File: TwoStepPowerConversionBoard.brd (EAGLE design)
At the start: 66 x 71.1 mm, 49 parts, among them U3 AZ1117EH-3.3TRG1

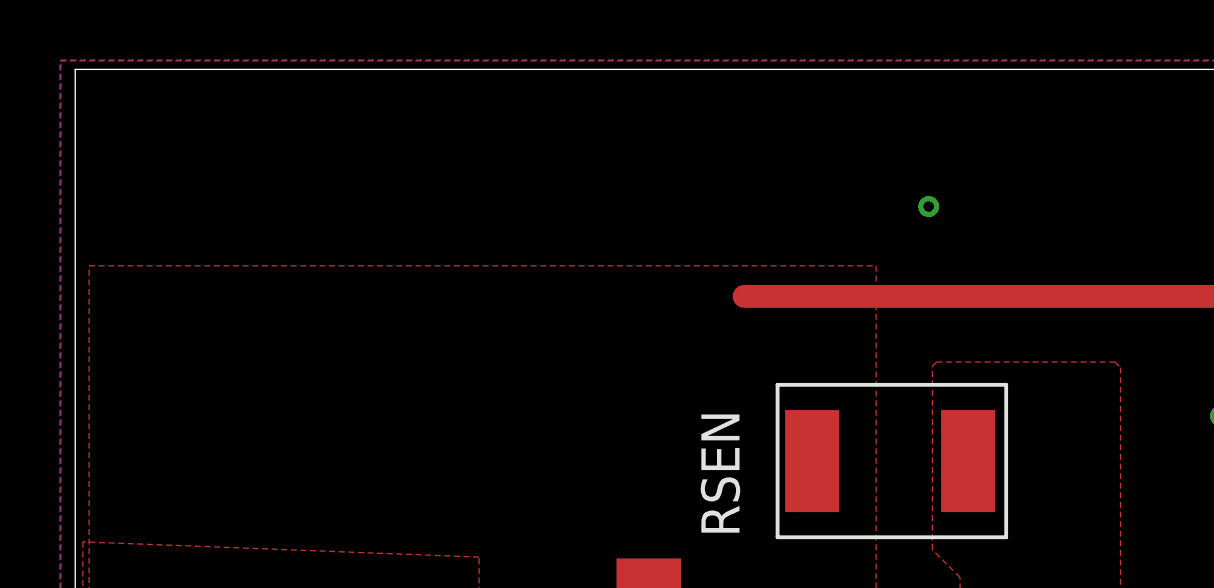
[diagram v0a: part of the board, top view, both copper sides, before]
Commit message: Larger LEDs on main and graphic and text on the other
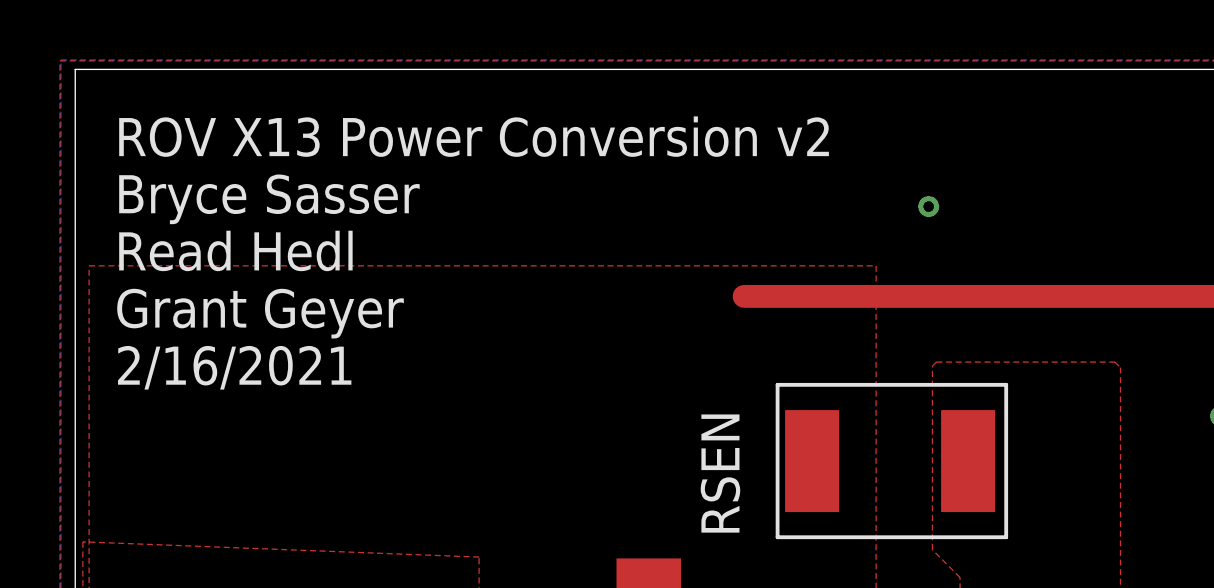
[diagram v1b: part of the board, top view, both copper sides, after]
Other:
- board text added: "ROV X13 Power Conversion v2 Bryce Sasser Read Hedl Grant Geyer 2/16/2021"
